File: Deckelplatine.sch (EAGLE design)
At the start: 71 parts, among them IC1 MAX1487EESA+, IC2 74HCT595D, IC3 74HCT595D, IC4 74HCT595D, IC5 74HCT595D, IC6 74HCT595D, J1 52808-2570, U1 LM2676S, X1 236-406/000-023, X2 233-502

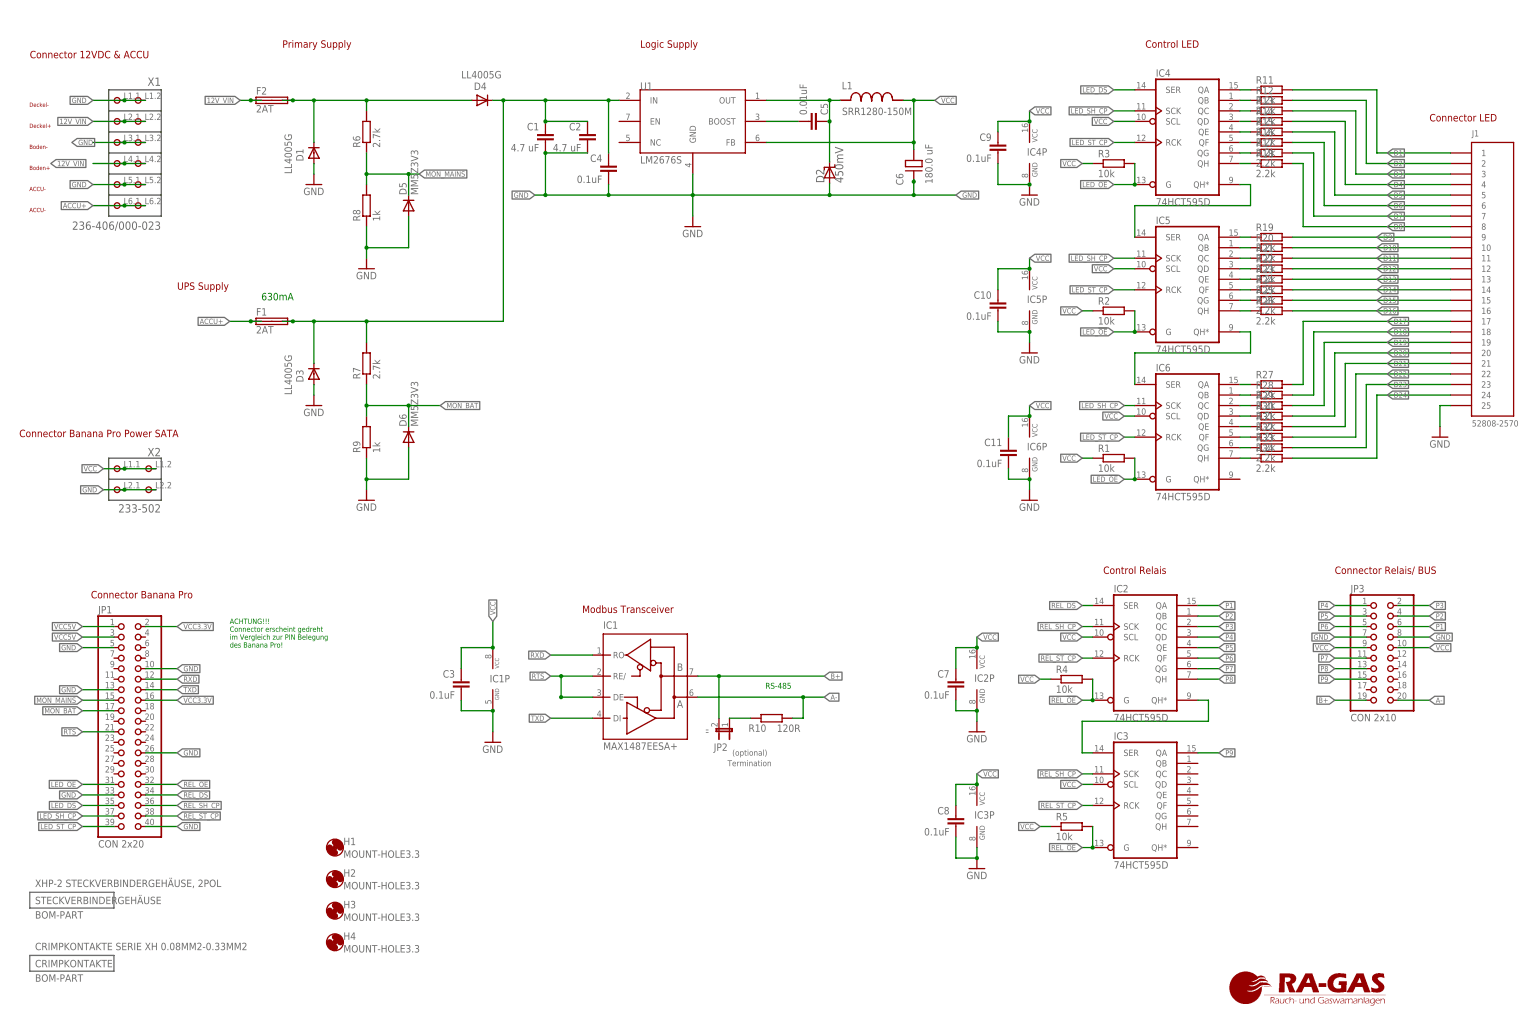
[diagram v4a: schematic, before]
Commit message: BOM und kontrolliert und eingfügt
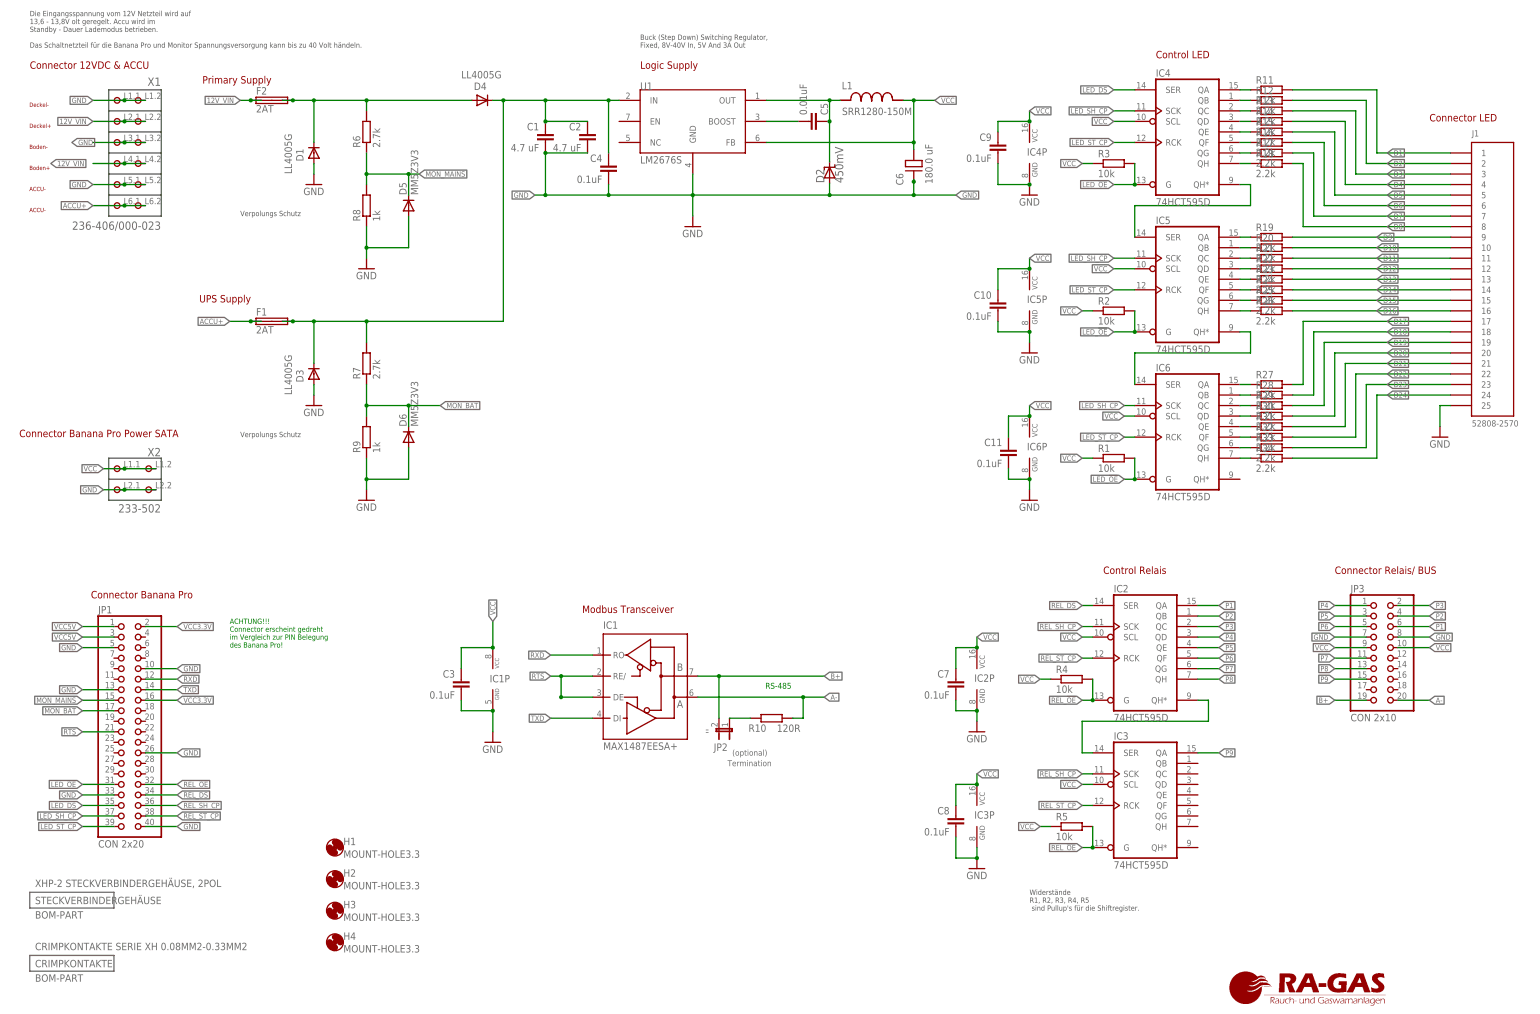
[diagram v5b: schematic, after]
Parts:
- X1: device con-wago_236:236-406/000-023 -> Deckelplatine:236-406/000-023
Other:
- note added: "Buck (Step Down) Switching Regulator, Fixed, 8V-40V In, 5V And 3A Out"
- note added: "Die Eingangsspannung vom 12V Netzteil wird auf 13,6 - 13,8V olt geregelt. Accu wird im Standby - Dauer Lademodus betrieben. Das Schaltnetzteil für die Banana Pro und Monitor Spannungsversorgung kann bis zu 40 Volt händeln."
- note added: "Verpolungs Schutz"
- note added: "Widerstände R1, R2, R3, R4, R5 sind Pullup's für die Shiftregister."
- note removed: "630mA"
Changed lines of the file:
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@@
 <attribute name="OC_FARNELL" value="1757123"/>
 </part>
-<part name="X1" library="con-wago_236" deviceset="236-406/000-023" device="" value="236-406/000-023">
+<part name="X1" library="Deckelplatine" deviceset="236-406/000-023" device="" value="236-406/000-023">
 <attribute name="DATASHEETURL" value="WAGO236_Connector Banana Pro Power SATA-WAGO236-402_WAGO236-403_WAGO236-404#WAG.pdf"/>
 <attribute name="MF" value="WAGO"/>
@@
 <text x="146.0246" y="109.9566" size="1.778" layer="94" font="vector" ratio="12">Modbus Transceiver</text>
 <text x="350.52" y="228.6" size="1.778" layer="94" font="vector" ratio="12">Connector LED</text>
-<text x="281.94" y="246.38" size="1.778" layer="94" font="vector" ratio="12">Control LED</text>
+<text x="284.48" y="243.84" size="1.778" layer="94" font="vector" ratio="12">Control LED</text>
 <text x="271.78" y="119.38" size="1.778" layer="94" font="vector" ratio="12">Control Relais</text>
-<text x="12.7" y="243.84" size="1.778" layer="94" font="vector" ratio="12">Connector 12VDC &amp; ACCU</text>
-<text x="48.26" y="187.96" size="1.778" layer="94" font="vector" ratio="12">UPS Supply</text>
-<text x="73.66" y="246.38" size="1.778" layer="94" font="vector" ratio="12">Primary Supply</text>
-<text x="160.02" y="246.38" size="1.778" layer="94" font="vector" ratio="12">Logic Supply</text>
+<text x="12.7" y="241.3" size="1.778" layer="94" font="vector" ratio="12">Connector 12VDC &amp; ACCU</text>
+<text x="53.594" y="184.912" size="1.778" layer="94" font="vector" ratio="12">UPS Supply</text>
+<text x="54.356" y="237.744" size="1.778" layer="94" font="vector" ratio="12">Primary Supply</text>
+<text x="160.02" y="241.3" size="1.778" layer="94" font="vector" ratio="12">Logic Supply</text>
 <text x="10.16" y="152.4" size="1.778" layer="94" font="vector" ratio="12">Connector Banana Pro Power SATA</text>
-<text x="68.58" y="185.42" size="1.778" layer="91">630mA</text>
 <text x="12.5984" y="211.7852" size="1.016" layer="94" font="vector">ACCU-</text>
 <text x="60.96" y="101.6" size="1.27" layer="91">ACHTUNG!!!
@@
 <text x="12.5984" y="232.1052" size="1.016" layer="94" font="vector">Deckel-</text>
 <text x="12.5984" y="227.0252" size="1.016" layer="94" font="vector">Deckel+</text>
+<text x="254" y="38.1" size="1.27" layer="97">Widerstände
+R1, R2, R3, R4, R5
+ sind Pullup's für die Shiftregister.</text>
+<text x="63.5" y="205.74" size="1.27" layer="97">Verpolungs Schutz</text>
+<text x="63.5" y="152.4" size="1.27" layer="97">Verpolungs Schutz</text>
+<text x="160.02" y="246.38" size="1.27" layer="97">Buck (Step Down) Switching Regulator,
+Fixed, 8V-40V In, 5V And 3A Out</text>
+<text x="12.7" y="246.38" size="1.27" layer="97">Die Eingangsspannung vom 12V Netzteil wird auf
+13,6 - 13,8V olt geregelt. Accu wird im
+Standby - Dauer Lademodus betrieben.
+Das Schaltnetzteil für die Banana Pro und Monitor Spannungsversorgung kann bis zu 40 Volt händeln.</text>
 </plain>
 <instances>

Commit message: Vergessener Commit zur Version 1.0.1
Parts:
- F1, F2: OC_FARNELL (none) -> 2413914
- IC1: OC_FARNELL_ALTERNATIVE (none) -> 8452210
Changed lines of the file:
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@@
 <attribute name="DATABASE" value="/home/smueller/eagle/_parts-database.txt.csv"/>
 <attribute name="PROJEKTNAME" value="xMZ-Mod-Touch-Deckelplatine"/>
-<attribute name="VERSION" value="0.9.5"/>
+<attribute name="VERSION" value="1.0.0"/>
 </attributes>
 <variantdefs>
@@
 <attribute name="MPN" value="MAX1487EESA+."/>
 <attribute name="OC_FARNELL" value="1593310"/>
+<attribute name="OC_FARNELL_ALTERNATIVE" value="8452210"/>
 <attribute name="PARTNO" value="MAX481CSA"/>
 </part>
@@
 <attribute name="MF" value="LITTELFUSE"/>
 <attribute name="MPN" value="01110005MR"/>
+<attribute name="OC_FARNELL" value="2413914"/>
 </part>
 <part name="U$1" library="xMZ-Mod-Touch-Bodenplatine" deviceset="LOGO_RA-GAS" device=""/>
@@
 <attribute name="MF" value="LITTELFUSE"/>
 <attribute name="MPN" value="01110005MR"/>
+<attribute name="OC_FARNELL" value="2413914"/>
 </part>
 <part name="D1" library="diode" deviceset="DIODE-" device="MELF-MLL41" value="LL4005G">
@@
 <attribute name="NAME" x="151.1046" y="106.1466" size="1.778" layer="95"/>
 <attribute name="VALUE" x="151.1046" y="76.9366" size="1.778" layer="96"/>
+<attribute name="OC_FARNELL_ALTERNATIVE" x="161.2646" y="92.1766" size="1.27" layer="96" display="off"/>
 </instance>
 <instance part="IC1" gate="P" x="124.46" y="93.98"/>
